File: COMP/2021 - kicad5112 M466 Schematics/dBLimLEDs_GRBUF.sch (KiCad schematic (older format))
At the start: 25 parts

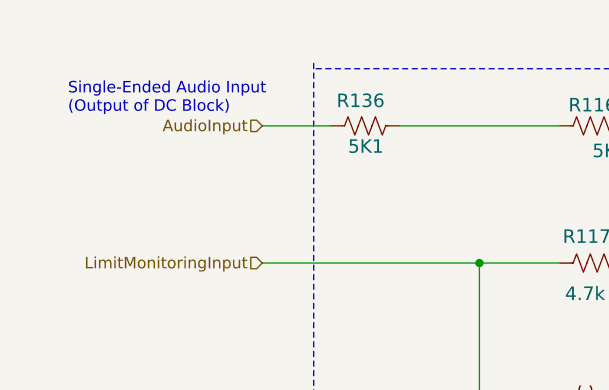
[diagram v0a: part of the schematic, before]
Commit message: Orignal M466 Schematic has been fully split and wired up into sub-schematic sheets corresponding to functional blocks.
Next steps:
	- Verify through simulation
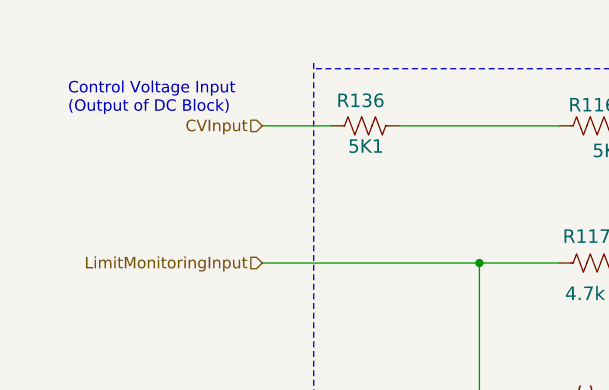
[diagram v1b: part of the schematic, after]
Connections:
- net AudioInput renamed CVInput
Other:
- note added: "Control Voltage Input\n(Output of DC Block)"
- note removed: "Single-Ended Audio Input\n(Output of DC Block)"
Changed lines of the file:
@@
 12dB\nYellow
 Text Notes 600  1025 0    50   ~ 0
-Single-Ended Audio Input\n(Output of DC Block)
+Control Voltage Input\n(Output of DC Block)
 Wire Wire Line
 	2400 1675 1450 1675
@@
 LimitMonitoringInput
 Text HLabel 1450 1075 0    50   Input ~ 0
-AudioInput
+CVInput
 $EndSCHEMATC
